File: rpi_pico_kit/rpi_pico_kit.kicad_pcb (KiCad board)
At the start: 2 copper layers, 99.1 x 99.1 mm, 256 parts, among them J1 DC Jack 5.5x2.1mm, J10 OLED Display SSD1306, J11 Conn_01x04_Male, J12 Conn_01x04_Male, J13 AudioJack-CUI-SJ-3523-SMT, J14 AudioJack-CUI-SJ-3523-SMT, J2 USB_B, J3 Conn_01x03_Male, J4 DB15_Female, J5 HDMI_A, J6 Conn_01x08_Male, J7 Conn_01x08_Male, J8 Conn_01x08_Male, J9 Micro_SD_Card_Det, Q1 DMN63D8L-7, Q2 DMN63D8L-7, Q3 DMN63D8L-7, Q4 DMN63D8L-7, Q5 DMN63D8L-7, Q6 DMN63D8L-7, Q7 DMN63D8L-7, SW1 SW_Push, SW10 SW_Push, SW2 RotaryEncoder_Switch, SW3 SW_Push, SW4 SW_Push, SW5 SW_Push, SW6 SW_Push, SW7 SW_Push, SW8 SW_Push, SW9 SW_Push, U1 RPi Pico, U10 74LVC2G34GV, U11 PCM5101A, U2 NCP1117-3.3_SOT223, U3 RP2040, U4 W25Q16JVSSIQ, U5 74HC14, U6 74HC14, U7 MCP23S08-xSO, U8 AT24CS32, U9 NCP115-3.3_SOT23-5, Y1 12MHz

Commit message: added resistor arrays to pcb
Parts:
- removed R10, R11, R12, R2, R25, R27, R28, R3, R30, R31, R33, R34, R36, R4, R41, R42, R43, R44, R5, R71, R72, R73, R74, R75, R76, R77, R78, R79, R80, R81, R82, R83, R84, R85, R86, R9: 1k, Resistor_SMD:R_0805_2012Metric_Pad1.20x1.40mm_HandSolder
- removed R26, R29, R32, R35: 10k, Resistor_SMD:R_0805_2012Metric_Pad1.20x1.40mm_HandSolder
- removed R45, R48, R50, R52: 2k, Resistor_SMD:R_0805_2012Metric_Pad1.20x1.40mm_HandSolder
- removed R63, R64, R65, R66, R67, R68, R69, R70: 270R, Resistor_SMD:R_0805_2012Metric_Pad1.20x1.40mm_HandSolder
- removed R88, R89, R90, R91: 4.7k, Resistor_SMD:R_0805_2012Metric_Pad1.20x1.40mm_HandSolder
- moved RN11 301.7 mm to (160.6, 111.3)
- moved RN9 301.7 mm to (160.6, 118.0)
- moved RN13 300.3 mm to (155.2, 111.3)
- moved RN4 298.9 mm to (159.5, 54.0)
- moved RN12 295.9 mm to (146.7, 121.5)
- moved RN5 293.4 mm to (170.4, 54.0)
- moved RN7 293.4 mm to (164.9, 54.0)
- moved RN6 293.3 mm to (159.5, 60.7)
- moved RN10 292.6 mm to (155.2, 118.0)
- moved TP3 254.5 mm to (81.1, -19.8)
- moved RN3 251.1 mm to (133.9, 17.7)
- moved RN8 245.8 mm to (131.4, 144.9)
- moved JP1 242.0 mm to (77.2, -16.9)
- moved C9 241.3 mm to (71.3, -20.1)
- moved TP2 239.9 mm to (80.9, -16.5)
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
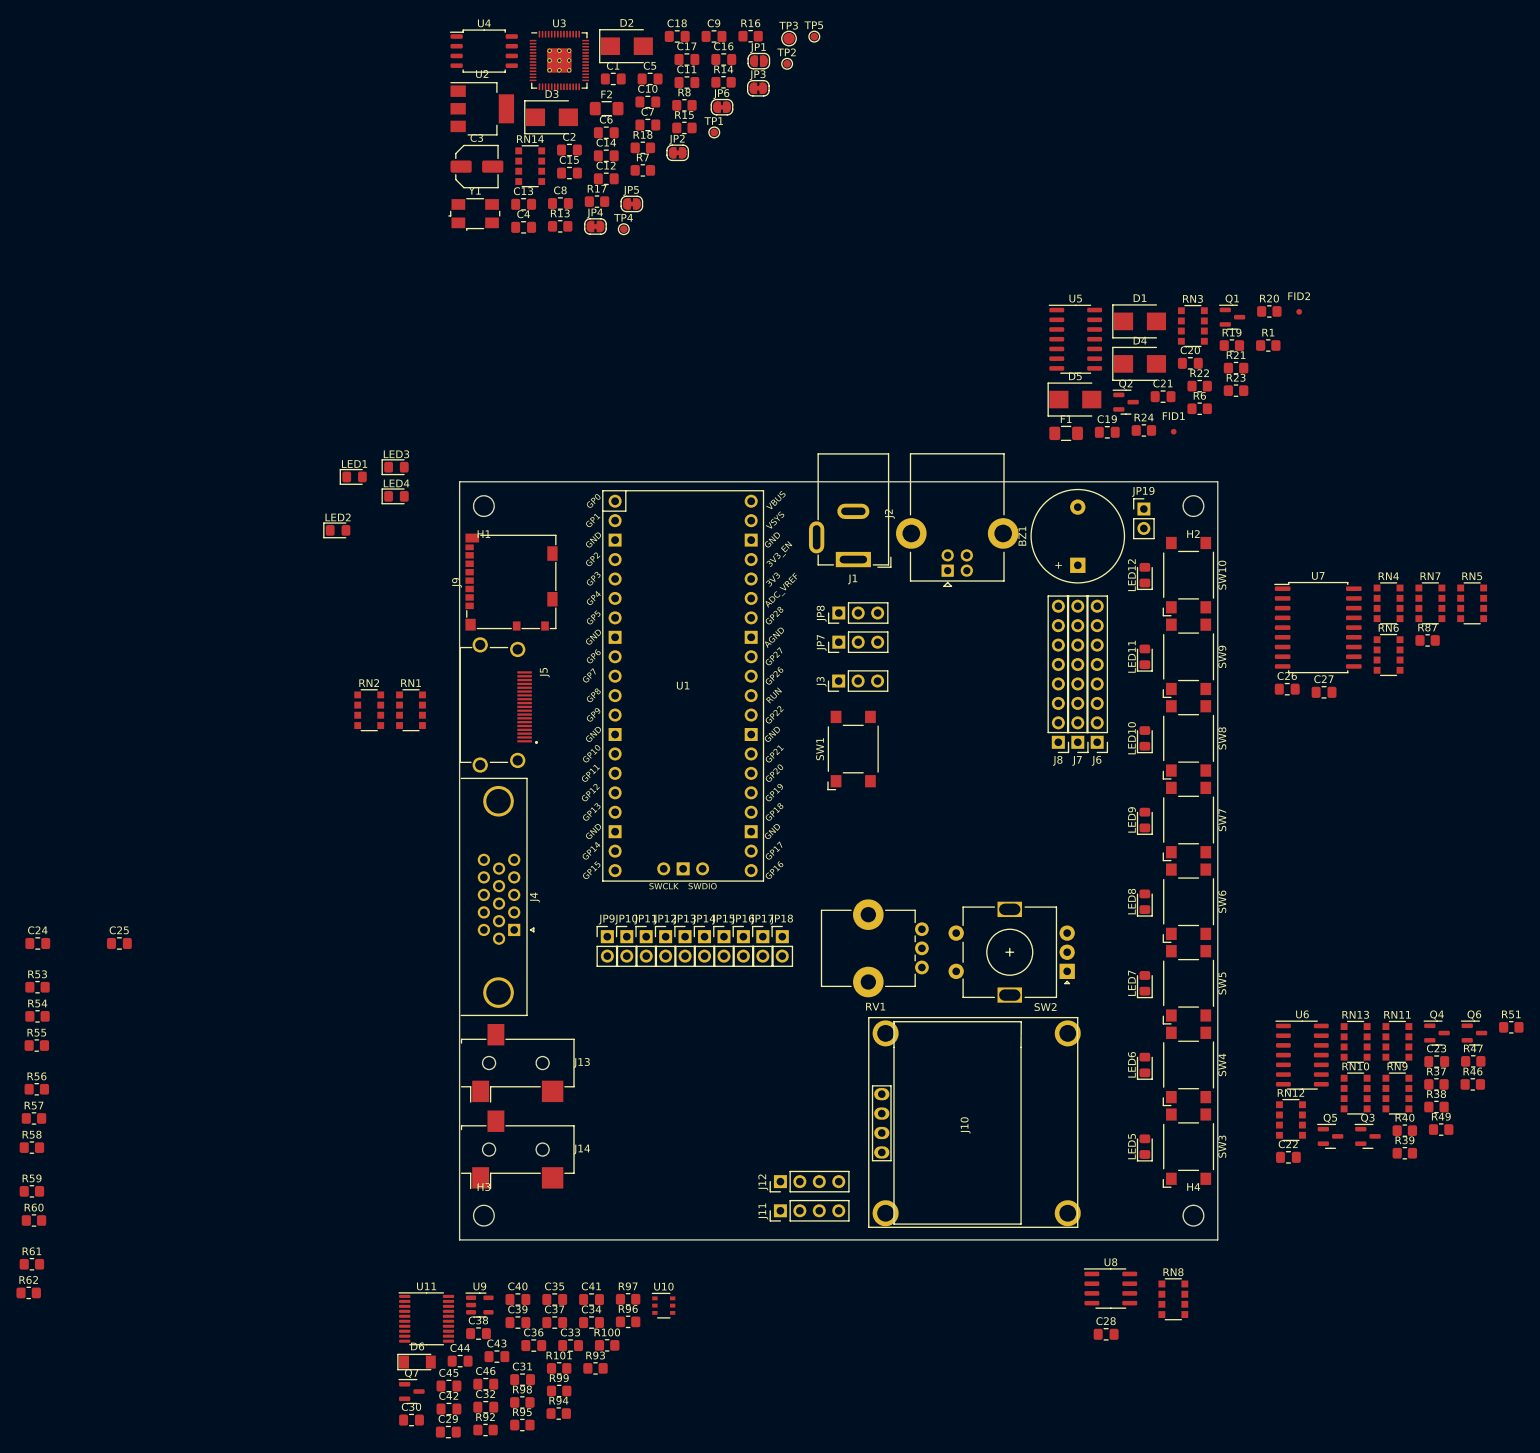
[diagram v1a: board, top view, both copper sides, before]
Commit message: changed footprints from 0805 to 0603
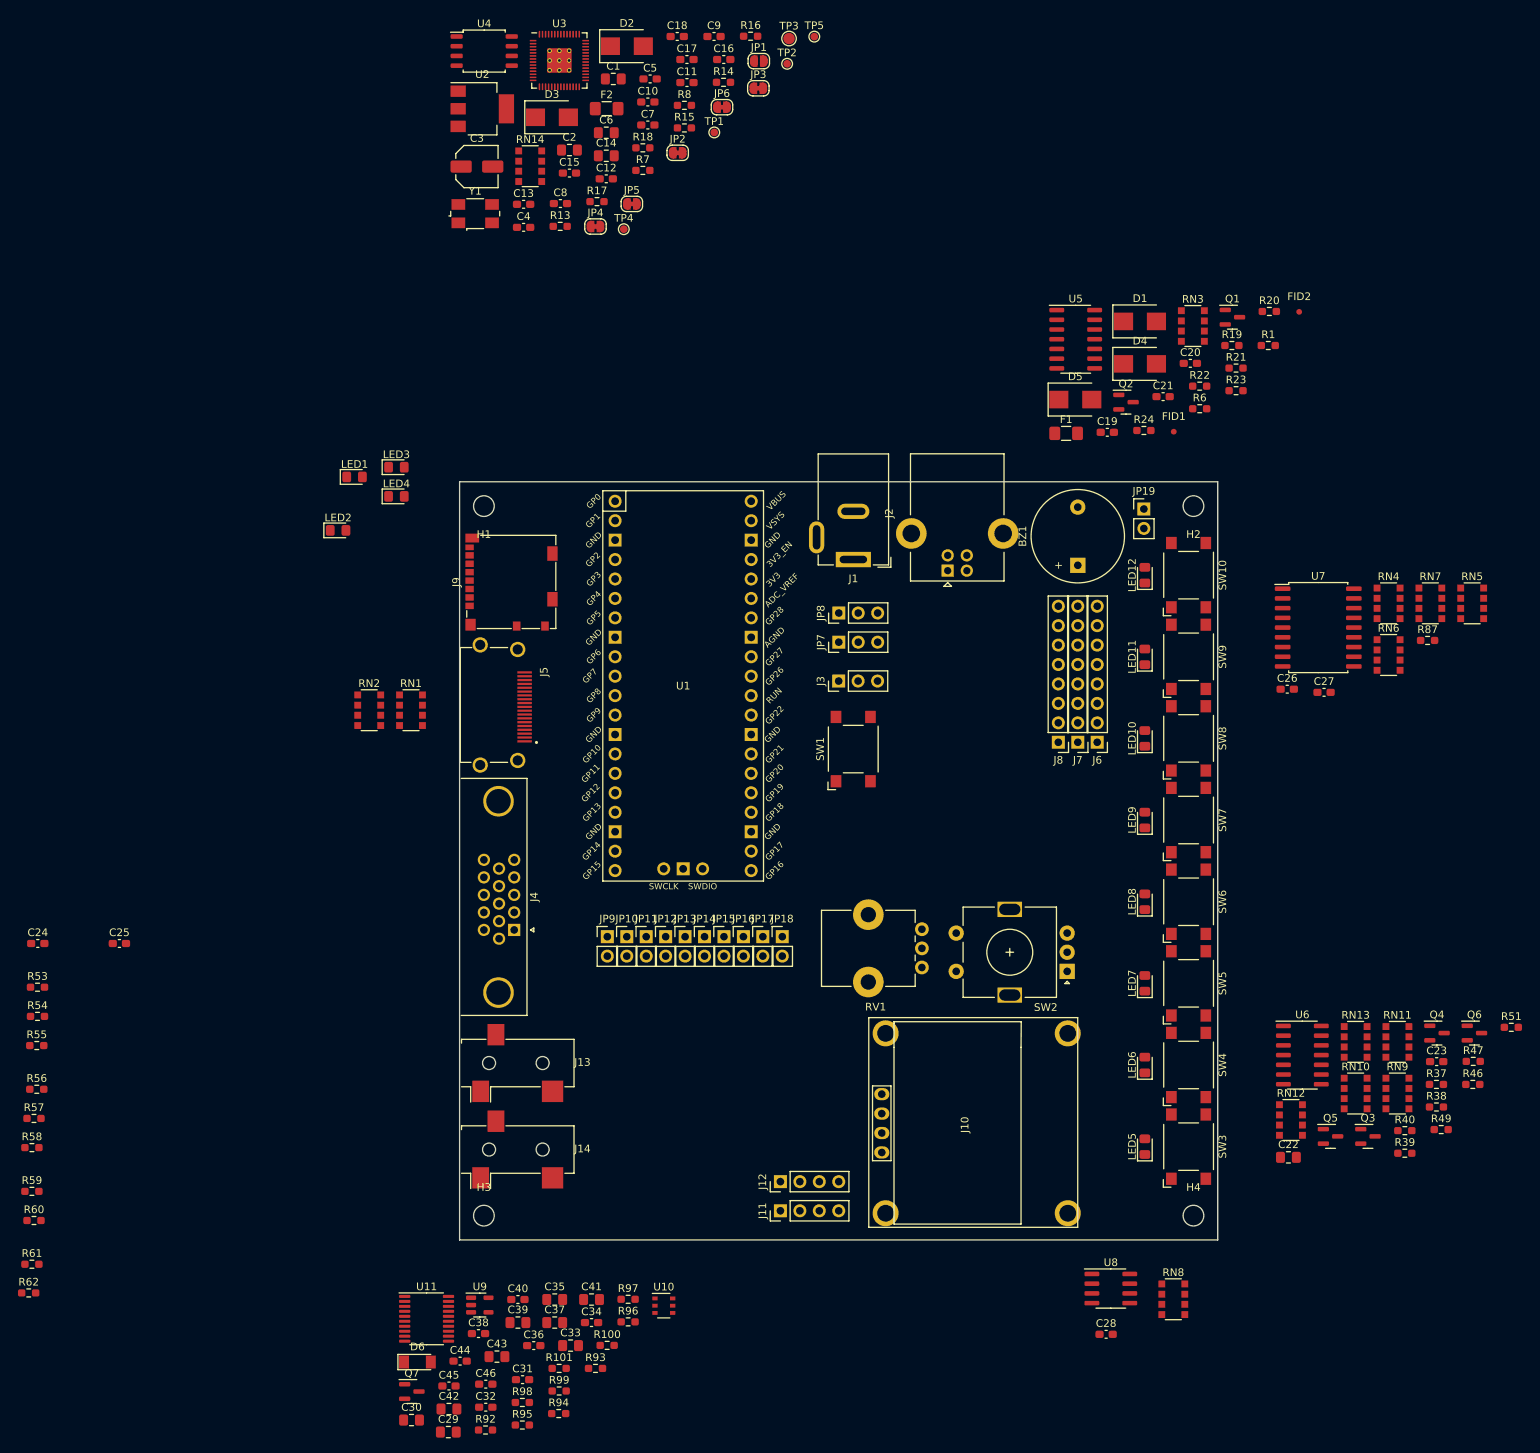
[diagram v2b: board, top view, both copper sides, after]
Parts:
- C10, C11, C12, C13, C15, C16, C17, C18, C19, C20, C21, C23, C24, C25, C26, C27, C28, C31, C32, C34, C36, C38, C4, C40, C44, C45, C46, C5, C7, C8, C9: footprint Capacitor_SMD:C_0805_2012Metric_Pad1.18x1.45mm_HandSolder -> Capacitor_SMD:C_0603_1608Metric_Pad1.08x0.95mm_HandSolder
- R1, R100, R101, R13, R14, R15, R16, R17, R18, R19, R20, R21, R22, R23, R24, R37, R38, R39, R40, R46, R47, R49, R51, R53, R54, R55, R56, R57, R58, R59, R6, R60, R61, R62, R7, R8, R87, R92, R93, R94, R95, R96, R97, R98, R99: footprint Resistor_SMD:R_0805_2012Metric_Pad1.20x1.40mm_HandSolder -> Resistor_SMD:R_0603_1608Metric_Pad0.98x0.95mm_HandSolder

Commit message: pcb changes
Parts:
- moved Q7 156.2 mm to (130.2, 35.6), turned to 90 degrees
- moved R101 140.1 mm to (125.9, 35.5), turned to 90 degrees
- moved R100 132.4 mm to (122.2, 35.5), turned to 90 degrees
- moved R62 106.0 mm to (80.0, 104.1), turned to -90 degrees
- moved R61 101.9 mm to (77.5, 104.1), turned to -90 degrees
- moved R60 97.3 mm to (74.9, 104.1), turned to -90 degrees
- moved R59 94.0 mm to (72.4, 104.1), turned to -90 degrees
- moved R58 90.0 mm to (69.8, 104.1), turned to -90 degrees
- moved R57 86.5 mm to (67.3, 104.1), turned to -90 degrees
- moved R56 83.0 mm to (64.8, 104.1), turned to -90 degrees
- moved R55 79.7 mm to (62.2, 104.1), turned to -90 degrees
- moved R54 76.8 mm to (59.7, 104.1), turned to -90 degrees
- moved R53 74.2 mm to (57.1, 104.1), turned to -90 degrees
- moved C25 69.9 mm to (51.4, 59.1)
- moved C24 67.3 mm to (49.5, 88.3), turned to -90 degrees
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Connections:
- JP17 pad 1: Net-(JP17-A) -> /DVI_D1-
- JP17 pad 2: /DVI_D1- -> Net-(JP17-B)
- JP18 pad 1: Net-(JP18-A) -> /VGA_VSYNC
- JP18 pad 2: /VGA_VSYNC -> Net-(JP18-B)
- R61 pad 1: Net-(J4-Pad13) -> Net-(JP17-B)
- R61 pad 2: Net-(JP17-A) -> Net-(J4-Pad13)
- R62 pad 1: Net-(J4-Pad14) -> Net-(JP18-B)
- R62 pad 2: Net-(JP18-A) -> Net-(J4-Pad14)
- RN1 pad 1: Net-(J5-D2+) -> Net-(J5-D1-)
- RN1 pad 2: Net-(J5-D2-) -> Net-(J5-D1+)
- RN1 pad 3: Net-(J5-D1+) -> Net-(J5-D2-)
- RN1 pad 4: Net-(J5-D1-) -> Net-(J5-D2+)
- RN1 pad 5: /DVI_D1- -> /DVI_D2+
- RN1 pad 6: /DVI_D1+ -> /DVI_D2-
- RN1 pad 7: /DVI_D2- -> /DVI_D1+
- RN1 pad 8: /DVI_D2+ -> /DVI_D1-
- RN2 pad 1: Net-(J5-D0+) -> Net-(J5-CK-)
- RN2 pad 2: Net-(J5-D0-) -> Net-(J5-CK+)
- RN2 pad 3: Net-(J5-CK+) -> Net-(J5-D0-)
- RN2 pad 4: Net-(J5-CK-) -> Net-(J5-D0+)
- RN2 pad 5: /DVI_CLK- -> /DVI_D0+
- RN2 pad 6: /DVI_CLK+ -> /DVI_D0-
- RN2 pad 7: /DVI_D0- -> /DVI_CLK+
- RN2 pad 8: /DVI_D0+ -> /DVI_CLK-
